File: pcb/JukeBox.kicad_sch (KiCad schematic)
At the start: 99 parts, among them J1 USB_C_Receptacle_USB2.0_16P, Q1 Q_NPN_BEC, SW1 SW_SPST, SW10 SW_SPST, SW11 SW_SPST, SW12 SW_SPST, SW13 SW_SPST, SW2 SW_SPST, SW3 SW_SPST, SW4 SW_SPST, SW5 SW_SPST, SW6 SW_SPST, SW7 SW_SPST, SW8 SW_SPST, SW9 SW_SPST, U1 NCP1117-3.3_SOT223, U2 W25Q128JVS, U3 RP2350_60QFN, U5 CAT24C512, Y1 ABM8-272-T3

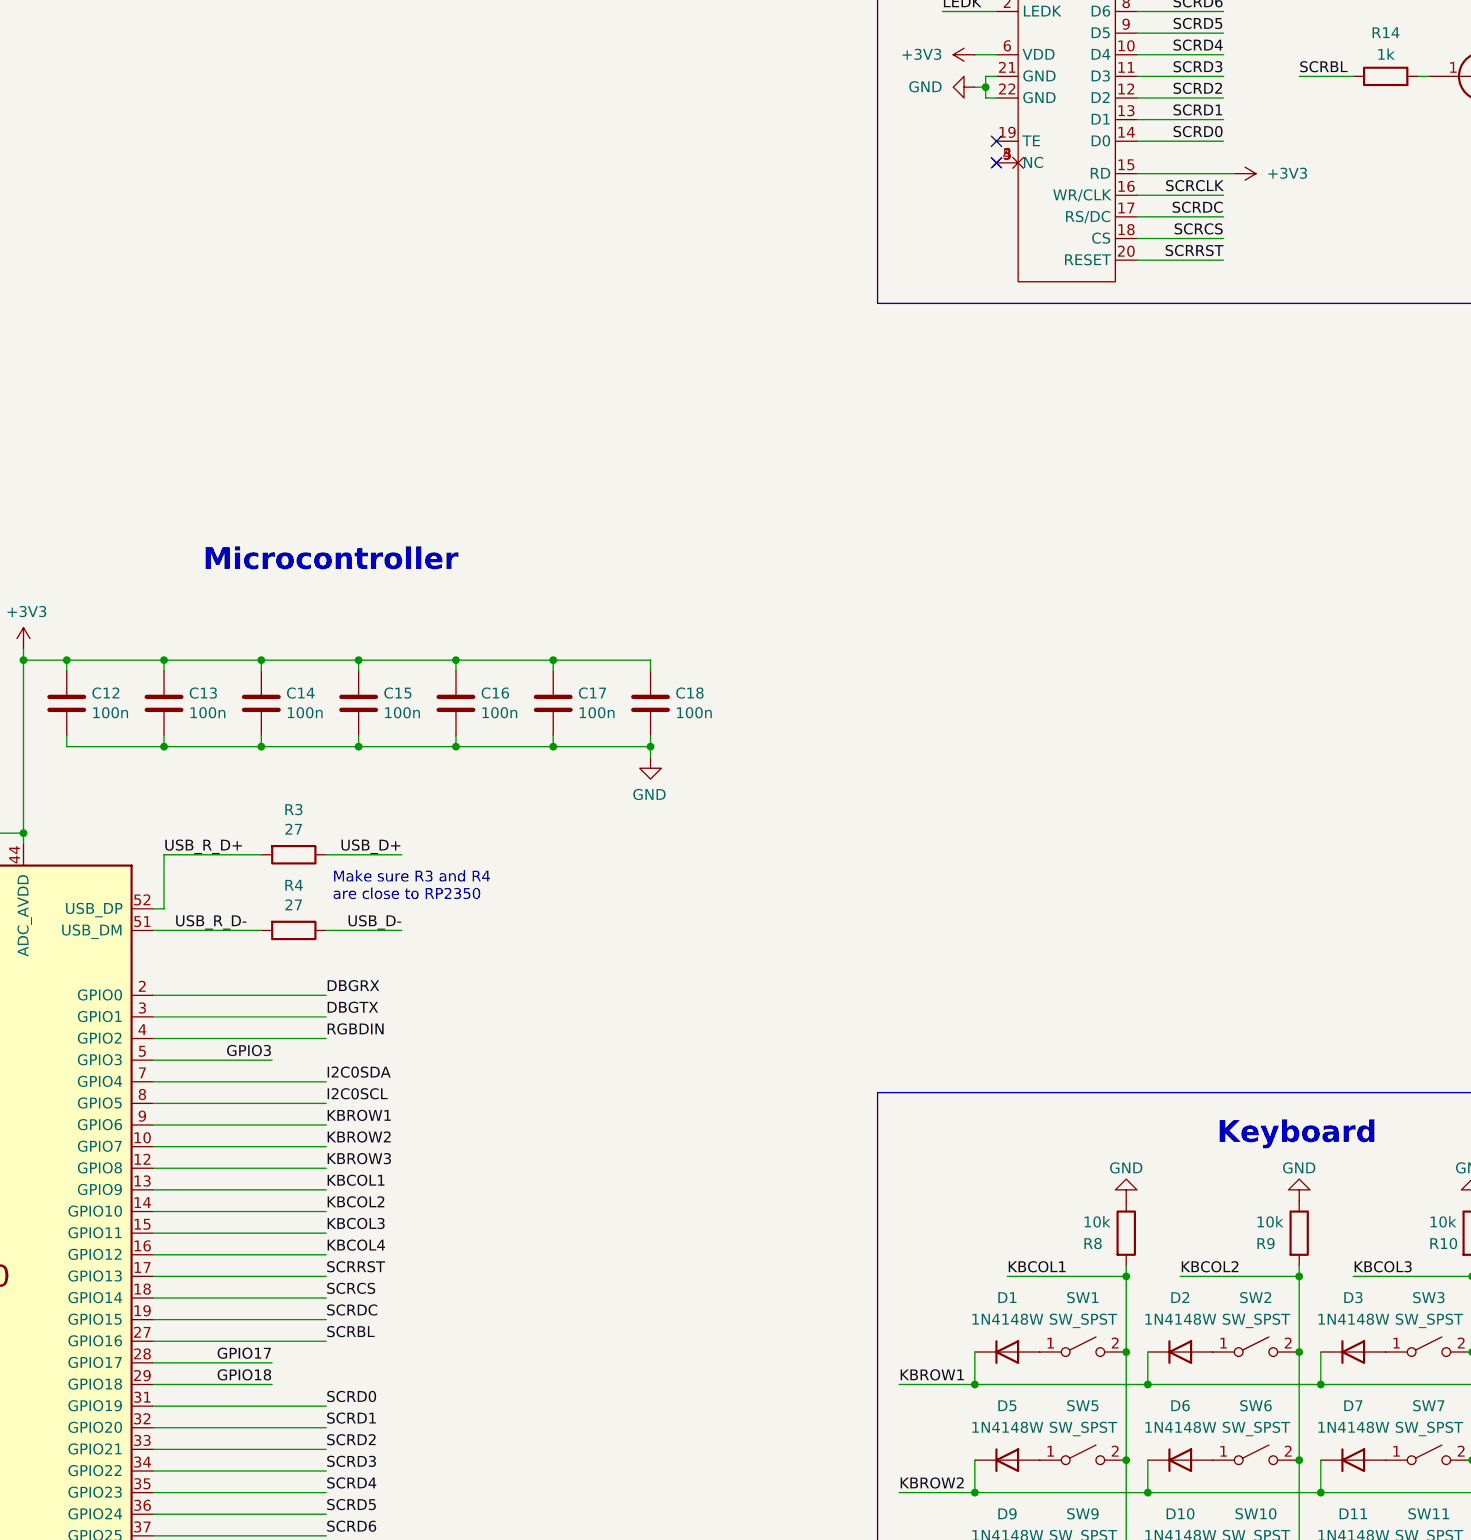
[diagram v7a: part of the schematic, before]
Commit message: update pcb to add missing pin for screen
ugh
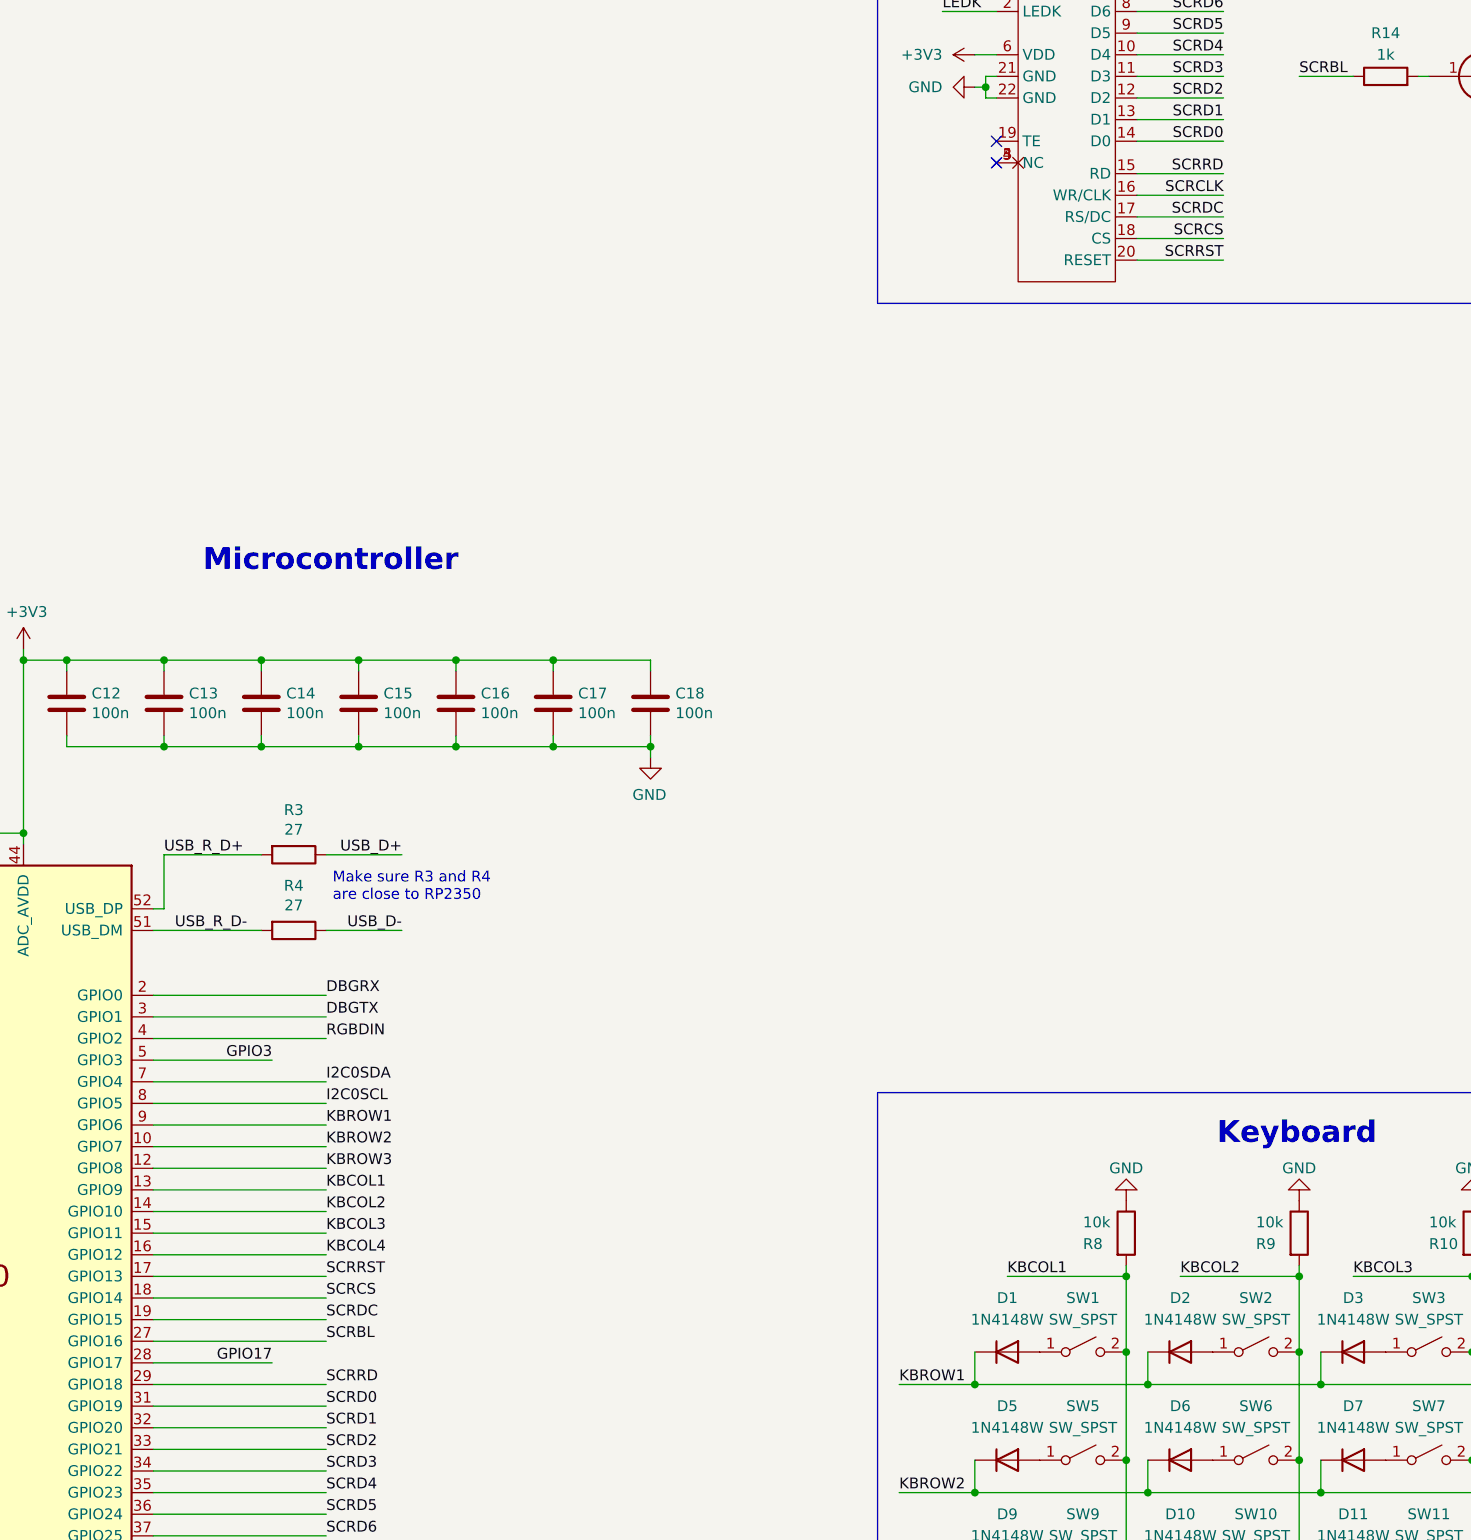
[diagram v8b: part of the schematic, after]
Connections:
- net +3V3: no longer U4.15 (RD)
- net GPIO18 renamed SCRRD
- net SCRRD: now also U4.15 (RD)
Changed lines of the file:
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@@
 	(wire
 		(pts
-			(xy 226.06 222.25) (xy 240.03 222.25)
+			(xy 226.06 222.25) (xy 246.38 222.25)
 		)
 		(stroke
@@
 	(wire
 		(pts
-			(xy 341.63 80.01) (xy 353.06 80.01)
-		)
-		(stroke
-			(width 0)
-			(type default)
-		)
-	)
-	(wire
-		(pts
 			(xy 124.46 39.37) (xy 124.46 40.64)
 		)
@@
 	(wire
 		(pts
+			(xy 341.63 80.01) (xy 351.79 80.01)
+		)
+		(stroke
+			(width 0)
+			(type default)
+		)
+	)
+	(wire
+		(pts
 			(xy 148.59 168.91) (xy 148.59 167.64)
 		)
@@
 		)
 	)
+	(label "SCRRD"
+		(at 351.79 80.01 180)
+		(effects
+			(font
+				(size 1.27 1.27)
+			)
+			(justify right bottom)
+		)
+	)
 	(label "KBCOL1"
 		(at 246.38 199.39 0)
@@
 		)
 	)
-	(label "GPIO18"
-		(at 240.03 222.25 180)
+	(label "SCRD2"
+		(at 246.38 229.87 0)
 		(effects
 			(font
 				(size 1.27 1.27)
 			)
-			(justify right bottom)
+			(justify left bottom)
 		)
 	)
-	(label "SCRD2"
-		(at 246.38 229.87 0)
+	(label "QSPI_SD2"
+		(at 151.13 196.85 0)
 		(effects
 			(font
@@
 		)
 	)
-	(label "QSPI_SD2"
-		(at 151.13 196.85 0)
+	(label "SCRRD"
+		(at 246.38 222.25 0)
 		(effects
 			(font
@@
 					(unit 1)
 				)
-			)
-		)
-	)
-	(symbol
-		(lib_id "power:+3V3")
-		(at 353.06 80.01 270)
-		(unit 1)
-		(exclude_from_sim no)
-		(in_bom yes)
-		(on_board yes)
-		(dnp no)
-		(fields_autoplaced yes)
-		(property "Reference" "#PWR16"
-			(at 349.25 80.01 0)
-			(effects
-				(font
-					(size 1.27 1.27)
-				)
-				(hide yes)
-			)
-		)
-		(property "Value" "+3V3"
-			(at 356.87 80.0099 90)
-			(effects
-				(font
-					(size 1.27 1.27)
-				)
-				(justify left)
-			)
-		)
-		(property "Footprint" ""
-			(at 353.06 80.01 0)
-			(effects
-				(font
-					(size 1.27 1.27)
-				)
-				(hide yes)
-			)
-		)
-		(property "Datasheet" ""
-			(at 353.06 80.01 0)
-			(effects
-				(font
-					(size 1.27 1.27)
-				)
-				(hide yes)
-			)
-		)
-		(property "Description" ""
-			(at 353.06 80.01 0)
-			(effects
-				(font
-					(size 1.27 1.27)
-				)
-				(hide yes)
-			)
-		)
-		(pin "1"
-		)
-		(instances
-			(project "JukeBox"
-				(path "/6328db6d-b3ae-4344-8bbe-195d6ec45eb3"
-					(reference "#PWR16")
-					(unit 1)
-				)
